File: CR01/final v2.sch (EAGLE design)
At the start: 41 parts, among them IC1 REG1117, IC2 TLE5205-2G, IC3 78D2T, Q1 IRFL024N\, Q2 IRFL024N\, U1 ATMEGA328P_TQFP, U2 SN74LVC2GU04DBVR

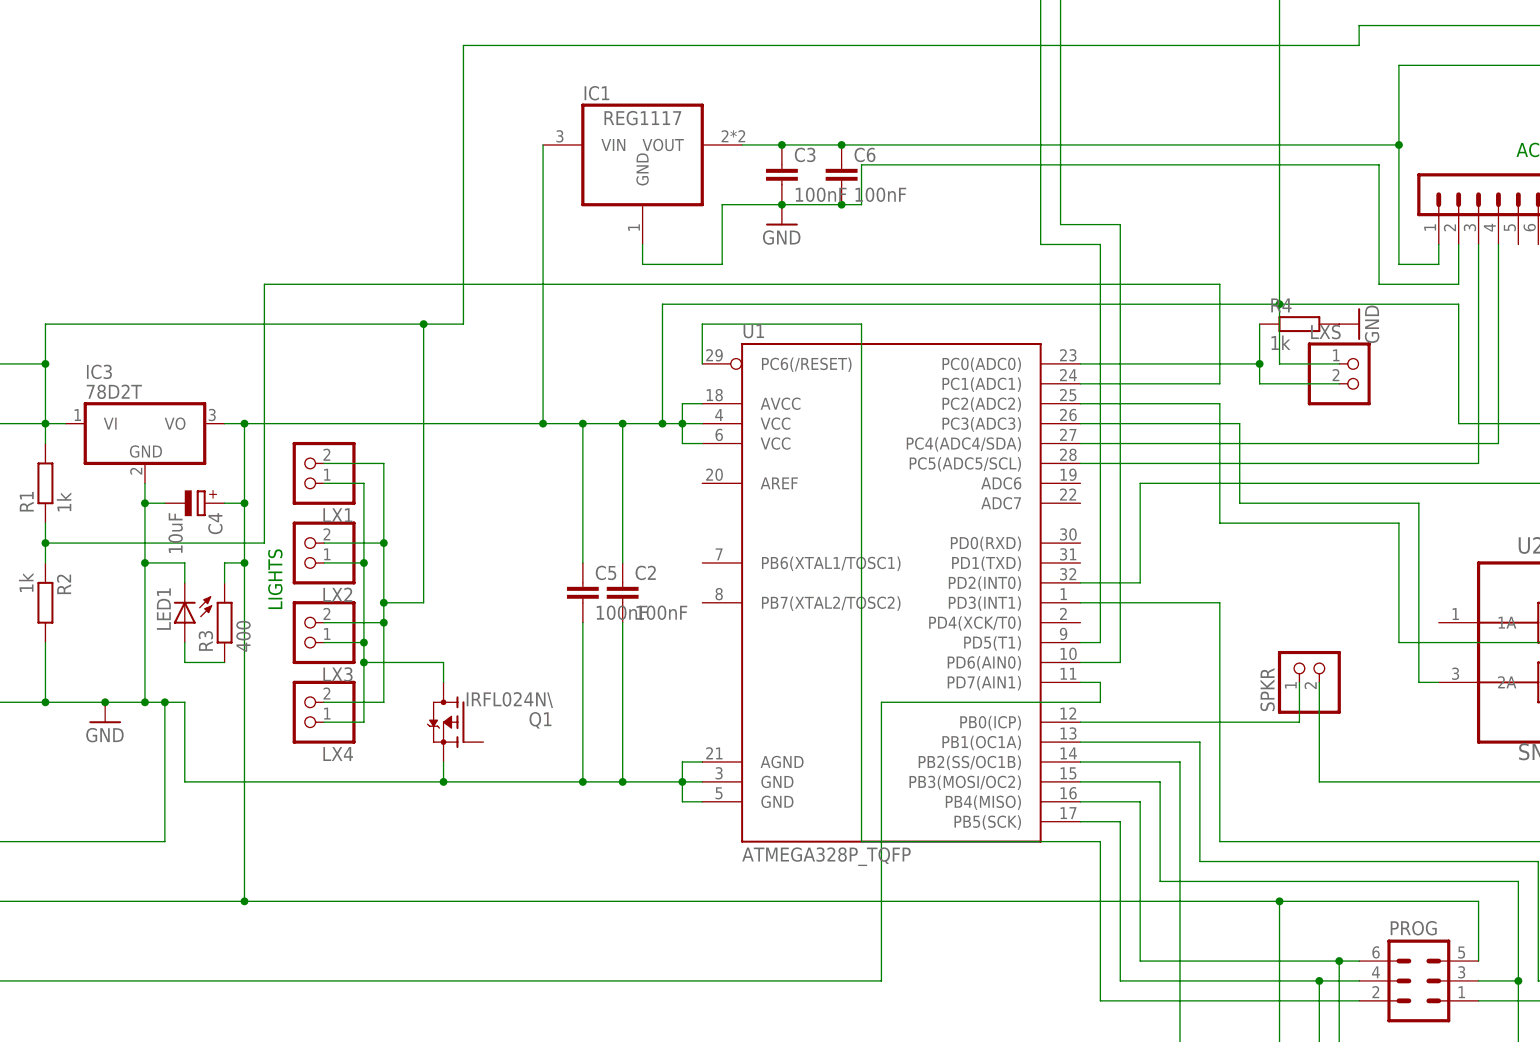
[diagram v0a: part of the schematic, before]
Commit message: Updated PCB and Schematic for V2.1
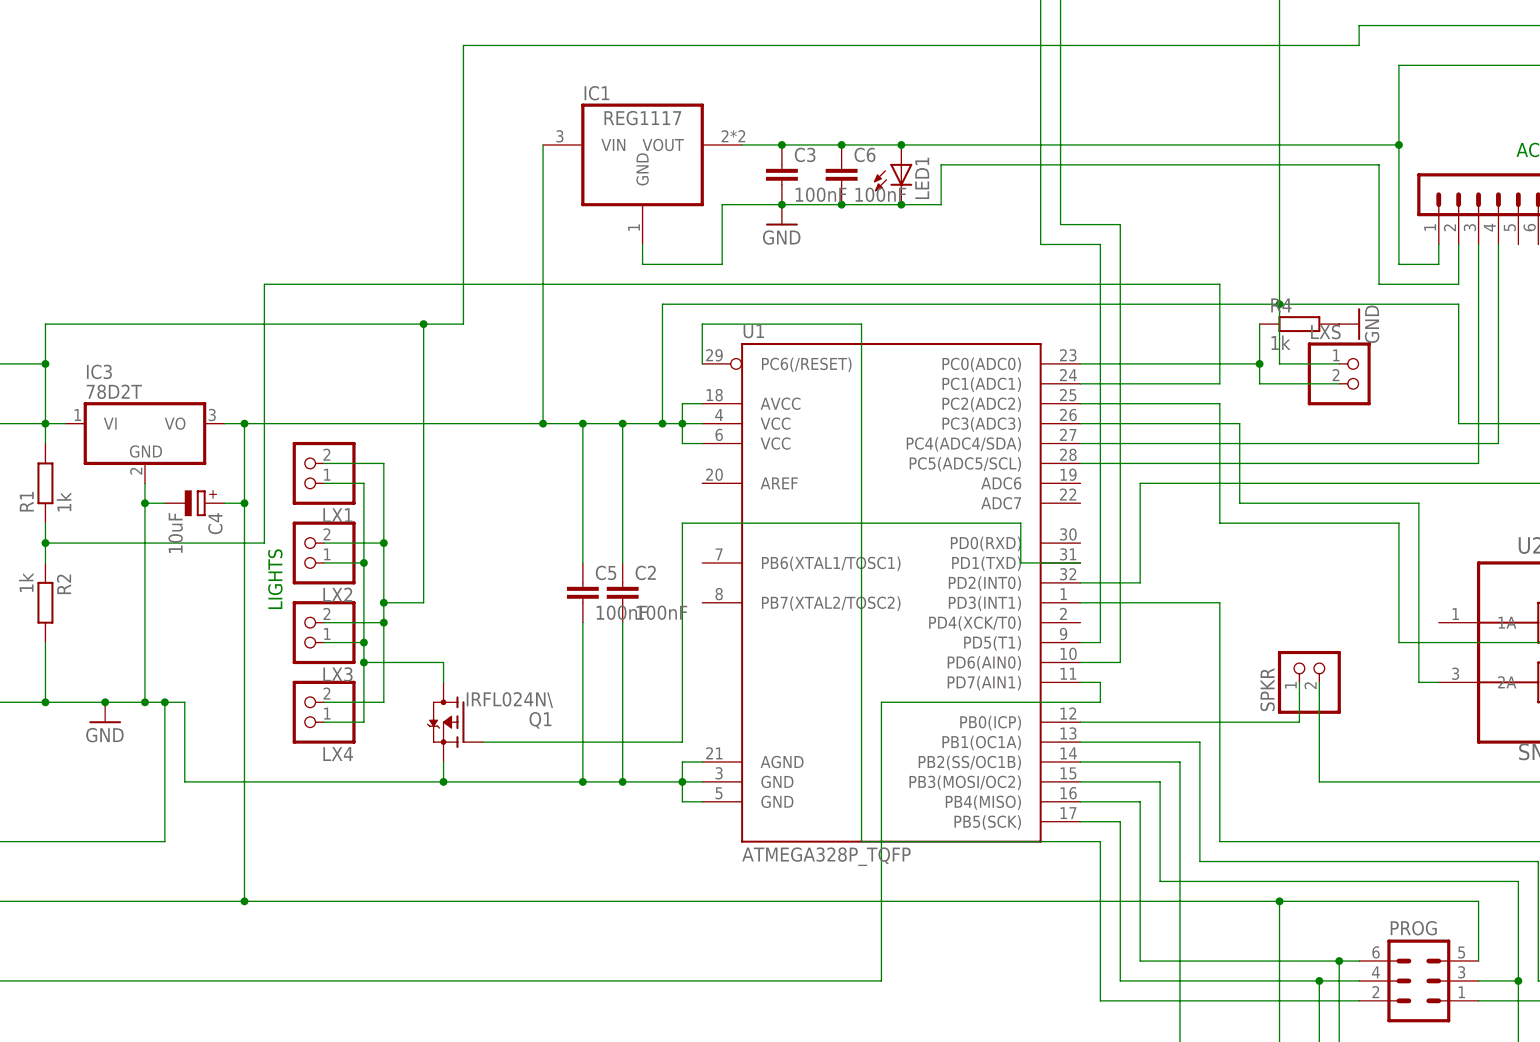
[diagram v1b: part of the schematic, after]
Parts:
- removed R3: 400, resistor:R-EU_R0603
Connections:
- removed net N$26: LED1.A, R3.1
- new net N$4: Q1.G, U1.PD1(TXD)
- net VCC: no longer R3.2
- net VCC2: now also LED1.A
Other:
- moved on the sheet: LED1
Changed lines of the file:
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@@
 <part name="C6" library="rcl" deviceset="C-EU" device="C1206" value="100nF"/>
 <part name="LED1" library="led" deviceset="LED" device="CHIPLED_0603"/>
-<part name="R3" library="resistor" deviceset="R-EU_" device="R0603" value="400"/>
 <part name="GND6" library="supply1" deviceset="GND" device=""/>
 </parts>
@@
 <instance part="C5" gate="G$1" x="60.96" y="40.64"/>
 <instance part="C6" gate="G$1" x="93.98" y="93.98"/>
-<instance part="LED1" gate="G$1" x="10.16" y="35.56" rot="R180"/>
-<instance part="R3" gate="G$1" x="15.24" y="35.56" rot="R90"/>
+<instance part="LED1" gate="G$1" x="101.6" y="93.98"/>
 <instance part="GND6" gate="1" x="86.36" y="86.36"/>
 </instances>
@@
 <wire x1="5.08" y1="25.4" x2="0" y2="25.4" width="0.1524" layer="91"/>
 <wire x1="5.08" y1="53.34" x2="5.08" y2="50.8" width="0.1524" layer="91"/>
-<wire x1="5.08" y1="50.8" x2="5.08" y2="43.18" width="0.1524" layer="91"/>
-<wire x1="5.08" y1="43.18" x2="5.08" y2="25.4" width="0.1524" layer="91"/>
+<wire x1="5.08" y1="50.8" x2="5.08" y2="25.4" width="0.1524" layer="91"/>
 <wire x1="7.62" y1="25.4" x2="7.62" y2="7.62" width="0.1524" layer="91"/>
 <junction x="5.08" y="25.4"/>
@@
 <wire x1="60.96" y1="35.56" x2="60.96" y2="15.24" width="0.1524" layer="91"/>
 <junction x="60.96" y="15.24"/>
-<pinref part="LED1" gate="G$1" pin="C"/>
-<wire x1="10.16" y1="40.64" x2="10.16" y2="43.18" width="0.1524" layer="91"/>
-<wire x1="10.16" y1="43.18" x2="5.08" y2="43.18" width="0.1524" layer="91"/>
-<junction x="5.08" y="43.18"/>
 <junction x="0" y="25.4"/>
 </segment>
@@
 <pinref part="C6" gate="G$1" pin="2"/>
 <junction x="93.98" y="88.9"/>
-<wire x1="96.52" y1="88.9" x2="93.98" y2="88.9" width="0.1524" layer="91"/>
-<wire x1="96.52" y1="93.98" x2="96.52" y2="88.9" width="0.1524" layer="91"/>
+<wire x1="106.68" y1="88.9" x2="101.6" y2="88.9" width="0.1524" layer="91"/>
+<wire x1="101.6" y1="88.9" x2="93.98" y2="88.9" width="0.1524" layer="91"/>
+<wire x1="106.68" y1="93.98" x2="106.68" y2="88.9" width="0.1524" layer="91"/>
 <pinref part="ACC" gate="1" pin="2"/>
 <wire x1="172.72" y1="83.82" x2="172.72" y2="78.74" width="0.1524" layer="91"/>
 <wire x1="172.72" y1="78.74" x2="162.56" y2="78.74" width="0.1524" layer="91"/>
 <wire x1="162.56" y1="78.74" x2="162.56" y2="93.98" width="0.1524" layer="91"/>
-<wire x1="162.56" y1="93.98" x2="96.52" y2="93.98" width="0.1524" layer="91"/>
+<wire x1="162.56" y1="93.98" x2="106.68" y2="93.98" width="0.1524" layer="91"/>
 <pinref part="GND6" gate="1" pin="GND"/>
+<pinref part="LED1" gate="G$1" pin="C"/>
+<junction x="101.6" y="88.9"/>
 </segment>
 </net>
@@
 <wire x1="15.24" y1="60.96" x2="17.78" y2="60.96" width="0.1524" layer="91"/>
 <wire x1="-17.78" y1="0" x2="17.78" y2="0" width="0.1524" layer="91"/>
-<wire x1="17.78" y1="0" x2="17.78" y2="43.18" width="0.1524" layer="91"/>
+<wire x1="17.78" y1="0" x2="17.78" y2="50.8" width="0.1524" layer="91"/>
 <junction x="17.78" y="0"/>
 <pinref part="PROG" gate="1" pin="5"/>
-<wire x1="17.78" y1="43.18" x2="17.78" y2="50.8" width="0.1524" layer="91"/>
 <wire x1="17.78" y1="50.8" x2="17.78" y2="60.96" width="0.1524" layer="91"/>
 <wire x1="17.78" y1="0" x2="149.86" y2="0" width="0.1524" layer="91"/>
@@
 <wire x1="60.96" y1="43.18" x2="60.96" y2="60.96" width="0.1524" layer="91"/>
 <junction x="60.96" y="60.96"/>
-<pinref part="R3" gate="G$1" pin="2"/>
-<wire x1="15.24" y1="40.64" x2="15.24" y2="43.18" width="0.1524" layer="91"/>
-<wire x1="15.24" y1="43.18" x2="17.78" y2="43.18" width="0.1524" layer="91"/>
-<junction x="17.78" y="43.18"/>
 </segment>
 </net>
@@
 <junction x="86.36" y="96.52"/>
 <pinref part="C6" gate="G$1" pin="1"/>
-<wire x1="93.98" y1="96.52" x2="165.1" y2="96.52" width="0.1524" layer="91"/>
+<wire x1="93.98" y1="96.52" x2="101.6" y2="96.52" width="0.1524" layer="91"/>
 <junction x="93.98" y="96.52"/>
+<pinref part="LED1" gate="G$1" pin="A"/>
+<wire x1="101.6" y1="96.52" x2="165.1" y2="96.52" width="0.1524" layer="91"/>
+<junction x="101.6" y="96.52"/>
 </segment>
 </net>
@@
 </segment>
 </net>
-<net name="N$26" class="0">
-<segment>
-<pinref part="R3" gate="G$1" pin="1"/>
-<pinref part="LED1" gate="G$1" pin="A"/>
-<wire x1="15.24" y1="30.48" x2="10.16" y2="30.48" width="0.1524" layer="91"/>
-<wire x1="10.16" y1="30.48" x2="10.16" y2="33.02" width="0.1524" layer="91"/>
-</segment>
-</net>
+<net name="N$4" class="0">
+<segment>
+<pinref part="Q1" gate="G$1" pin="G"/>
+<wire x1="48.26" y1="20.32" x2="73.66" y2="20.32" width="0.1524" layer="91"/>
+<wire x1="73.66" y1="20.32" x2="73.66" y2="48.26" width="0.1524" layer="91"/>
+<wire x1="73.66" y1="48.26" x2="116.84" y2="48.26" width="0.1524" layer="91"/>
+<wire x1="116.84" y1="48.26" x2="116.84" y2="43.18" width="0.1524" layer="91"/>
+<pinref part="U1" gate="U$1" pin="PD1(TXD)"/>
+<wire x1="116.84" y1="43.18" x2="124.46" y2="43.18" width="0.1524" layer="91"/>
+</segment>
+</net>

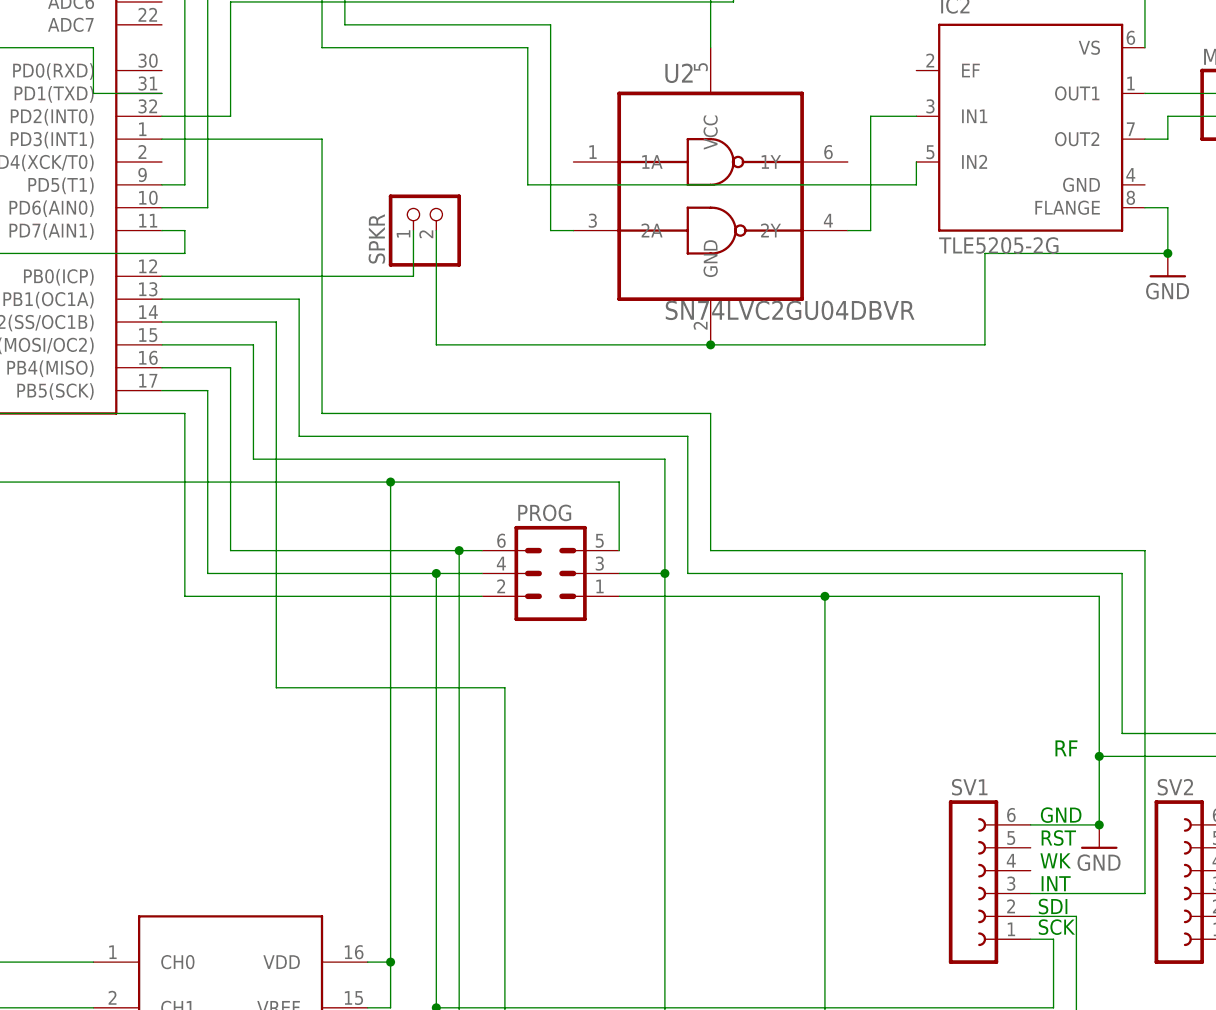
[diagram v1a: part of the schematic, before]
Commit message: Added controller testing program, reworked motor control library, perormed some unsuccessful testing
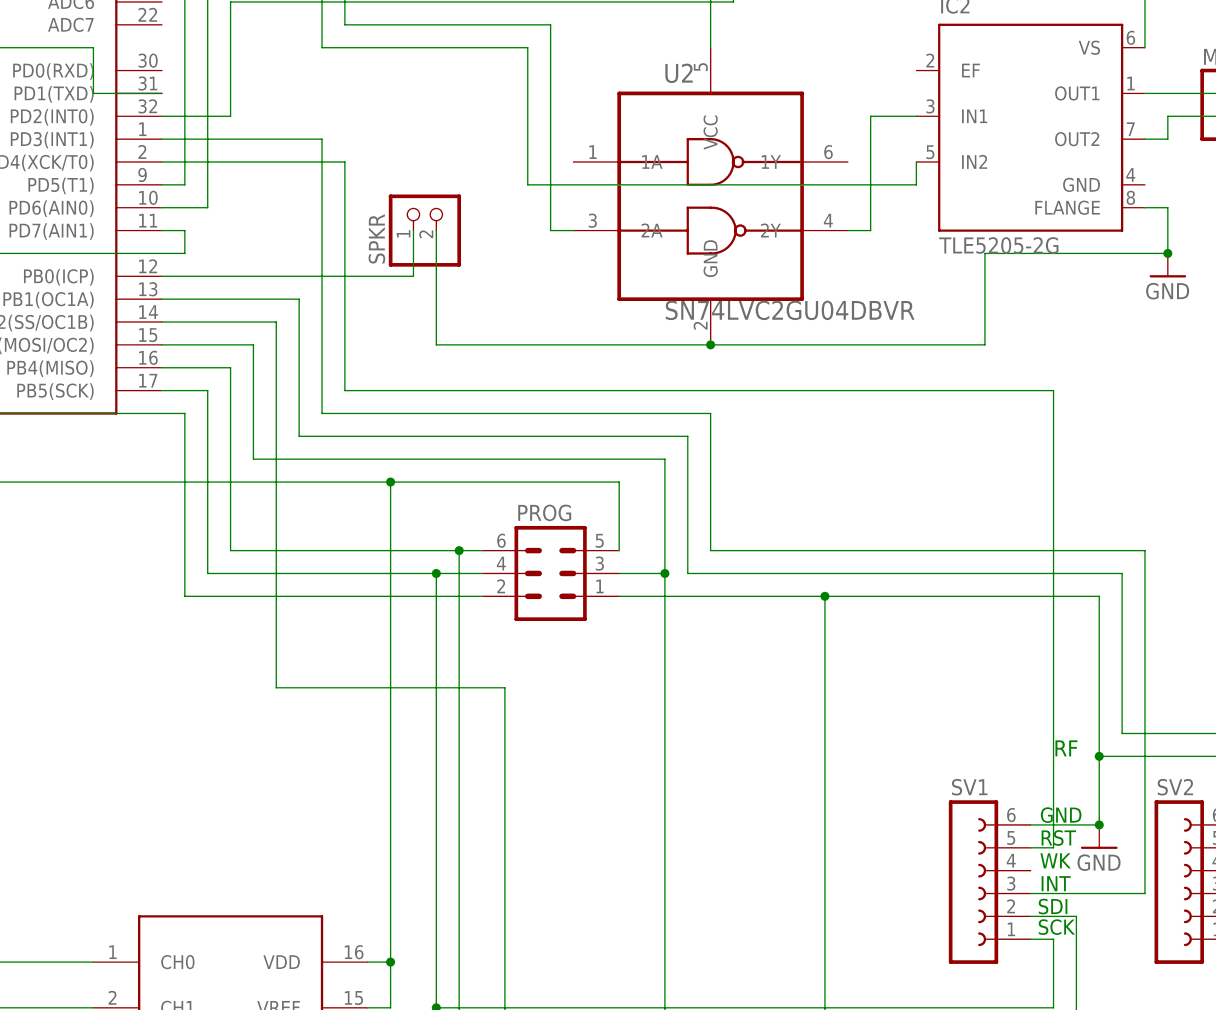
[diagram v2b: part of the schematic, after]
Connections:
- new net N$26: SV1.5, U1.PD4(XCK/T0)
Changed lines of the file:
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@@
+</segment>
+</net>
+<net name="N$26" class="0">
+<segment>
+<pinref part="SV1" gate="G$1" pin="5"/>
+<wire x1="220.98" y1="-40.64" x2="223.52" y2="-40.64" width="0.1524" layer="91"/>
+<wire x1="223.52" y1="-40.64" x2="223.52" y2="10.16" width="0.1524" layer="91"/>
+<wire x1="223.52" y1="10.16" x2="144.78" y2="10.16" width="0.1524" layer="91"/>
+<wire x1="144.78" y1="10.16" x2="144.78" y2="35.56" width="0.1524" layer="91"/>
+<pinref part="U1" gate="U$1" pin="PD4(XCK/T0)"/>
+<wire x1="144.78" y1="35.56" x2="124.46" y2="35.56" width="0.1524" layer="91"/>
 </segment>
 </net>

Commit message: final
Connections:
- net N$10 renamed RF_CS
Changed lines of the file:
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@@
 <?xml version="1.0" encoding="utf-8"?>
 <!DOCTYPE eagle SYSTEM "eagle.dtd">
-<eagle version="7.7.0">
+<eagle version="8.4.1">
 <drawing>
 <settings>
 <setting alwaysvectorfont="no"/>
+<setting keepoldvectorfont="yes"/>
 <setting verticaltext="up"/>
 </settings>
@@
 </segment>
 </net>
-<net name="N$10" class="0">
+<net name="RF_CS" class="0">
 <segment>
 <pinref part="U1" gate="U$1" pin="PB1(OC1A)"/>
